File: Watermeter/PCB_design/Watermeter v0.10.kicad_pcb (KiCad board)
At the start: 2 copper layers, 66.3 x 34.8 mm, 38 parts, among them P1 CONN_02X03, U1 AP1117D50, U2 AP1117D33, U3 ATSHA240A, U4 AT25DF512C, U5 TCRT5000, U6 LM393, U7 SI7021

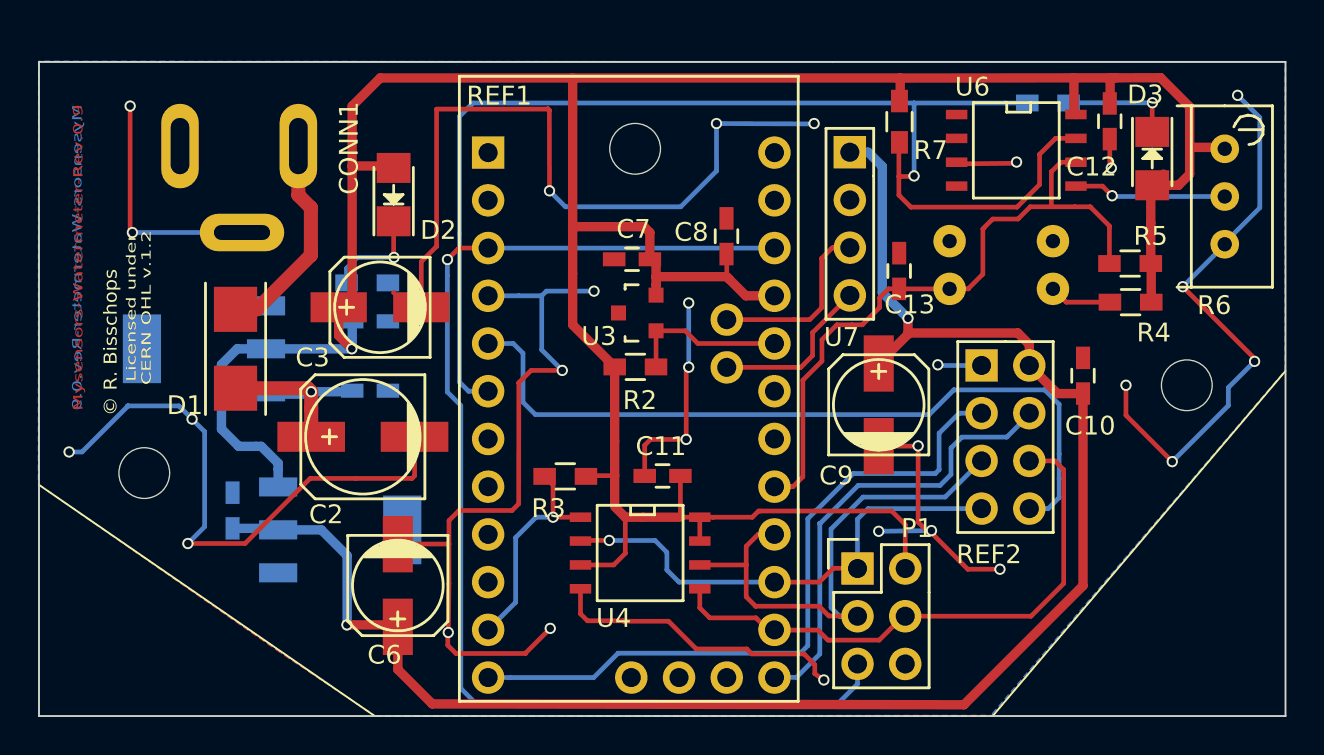
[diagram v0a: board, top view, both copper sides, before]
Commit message: Changes to schematics. Added andchanged components
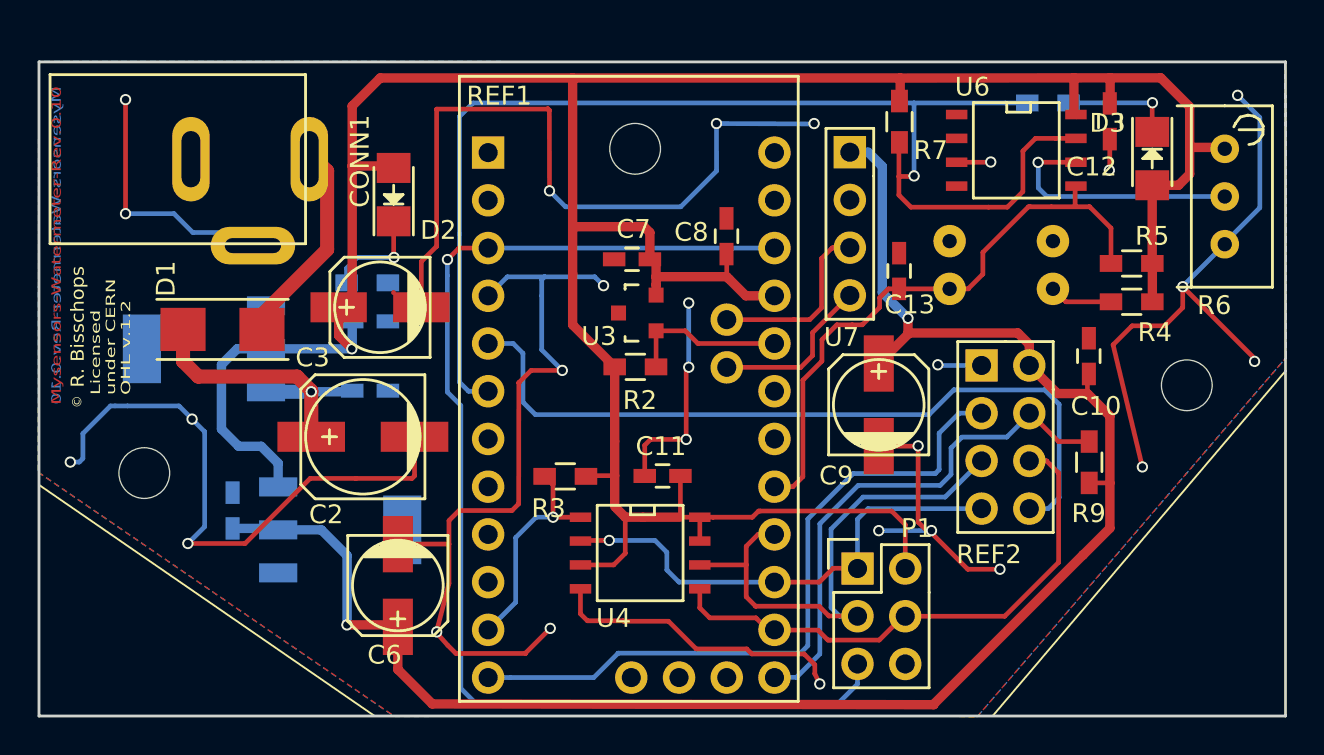
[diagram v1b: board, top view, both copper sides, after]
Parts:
- added R9: 56K, Resistors_SMD:R_0603_HandSoldering, F.Cu at (79.3, 62.2)
- D2, D3: footprint LEDs:LED_1206 -> MySensors:LED_1206
- R1: value 470 -> 1K
- R4: value 1K -> 180
- moved D1 1.24 mm to (33.2, 55.1), turned to 0 degrees
- moved C10 1.09 mm to (79.3, 56.5)
- moved CONN1 0.91 mm to (37.6, 50.6)
- moved R5 0.08 mm to (81.6, 51.6)
- moved R4 0.06 mm to (81.6, 53.7)
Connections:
- REF1 pad 1: (no net) -> Net-(REF1-Pad1)
- REF1 pad 10: (no net) -> Net-(REF1-Pad10)
- REF1 pad 18: (no net) -> Net-(REF1-Pad18)
- REF1 pad 19: (no net) -> Net-(REF1-Pad19)
- REF1 pad 2: (no net) -> Net-(REF1-Pad2)
- REF1 pad 24: (no net) -> Net-(REF1-Pad24)
- REF1 pad 33: (no net) -> Net-(REF1-Pad33)
- REF1 pad 34: (no net) -> Net-(REF1-Pad34)
- REF1 pad 7: (no net) -> Net-(REF1-Pad7)
- REF1 pad 8: (no net) -> Net-(REF1-Pad8)
- REF1 pad 9: (no net) -> Net-(REF1-Pad9)
- U6 pad 1: (no net) -> Net-(U6-Pad1)
- U6 pad 5: Net-(R6-Pad2) -> A0
- U6 pad 6: A0 -> Net-(R6-Pad2)
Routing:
- net Net-(R6-Pad2): track 8.15 -> 13.5 mm
- net Net-(C1-Pad1): track 11.1 -> 16.2 mm
- net RAD_CSN: track 24.4 -> 28.1 mm
- net A0: track 35.2 -> 32.2 mm
- net GND: track 200.1 -> 202.9 mm, vias 28 -> 27
- net +3.3V: track 91.9 -> 94.4 mm
- net MOSI: track 30.8 -> 29.5 mm
- net VCC: track 166.1 -> 165.0 mm
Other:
- outline, holes or cut-outs redrawn
- board text added: "Mysensors-Watermeter-Rev.0.10"
- board text added: "R. Bisschops"
- board text added: "©"
- board text removed: "Mysensors-Watermeter-Rev.0.9"
- board text removed: "© R. Bisschops"
